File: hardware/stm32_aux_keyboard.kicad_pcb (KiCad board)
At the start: 2 copper layers, 95 x 95 mm, 188 parts, among them J1 I2C_HEADER,2.54, J2 WS2812_HEADER, J3 BUZZER_HEADER, J4 ROT_ENC_HEADER, J5 SWD_SWD, J6 SWD_SWD, J7 ROT_ENC_HEADER, J8 I2C_HEADER,2.54, Q1 SS9013_J3, SW1 USR_BTN_1, SW10 KEY22, SW11 KEY23, SW12 KEY31, SW13 KEY32, SW14 KEY33, SW18 ROT1, SW19 SW_RESET,2_leg,SMD, SW2 USR_BTN_2, SW3 USR_BTN_3, SW5 ROT2, SW6 KEY11, SW7 KEY12, SW8 KEY13, SW9 KEY21, U1 SSD1306-OLED-I2C, U10 STM32F103C8T6, U2 AMS1117-3.3, U3 74AHCT1G125, U4 USB, U5 USBLC6-2SC6_SOT23-6, U6 STM32F103C8T6_rect, U7 SWD, U8 AMS1117-3.3, U9 USBLC6-2SC6_SOT23-6, Y1 O_8M, Y2 O8M, Y3 O32.768K

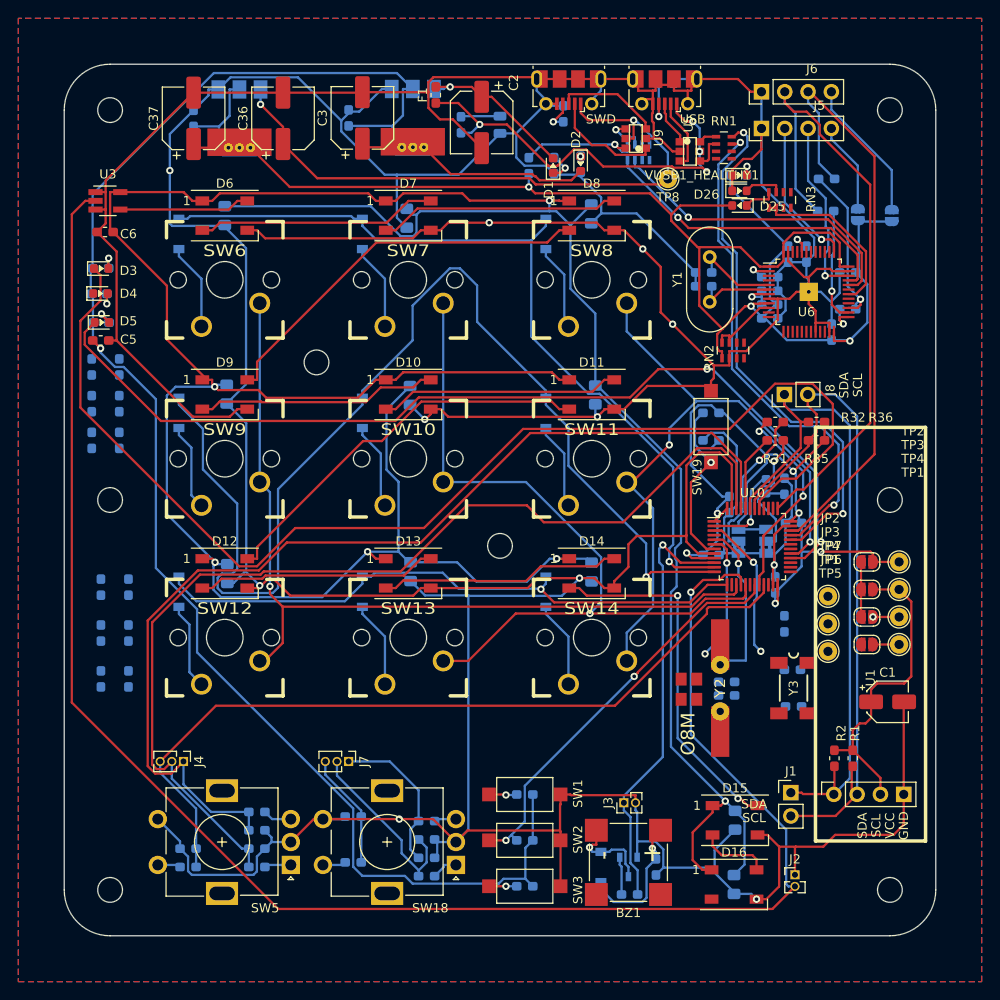
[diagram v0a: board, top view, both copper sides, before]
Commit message: update for tidy tracks,
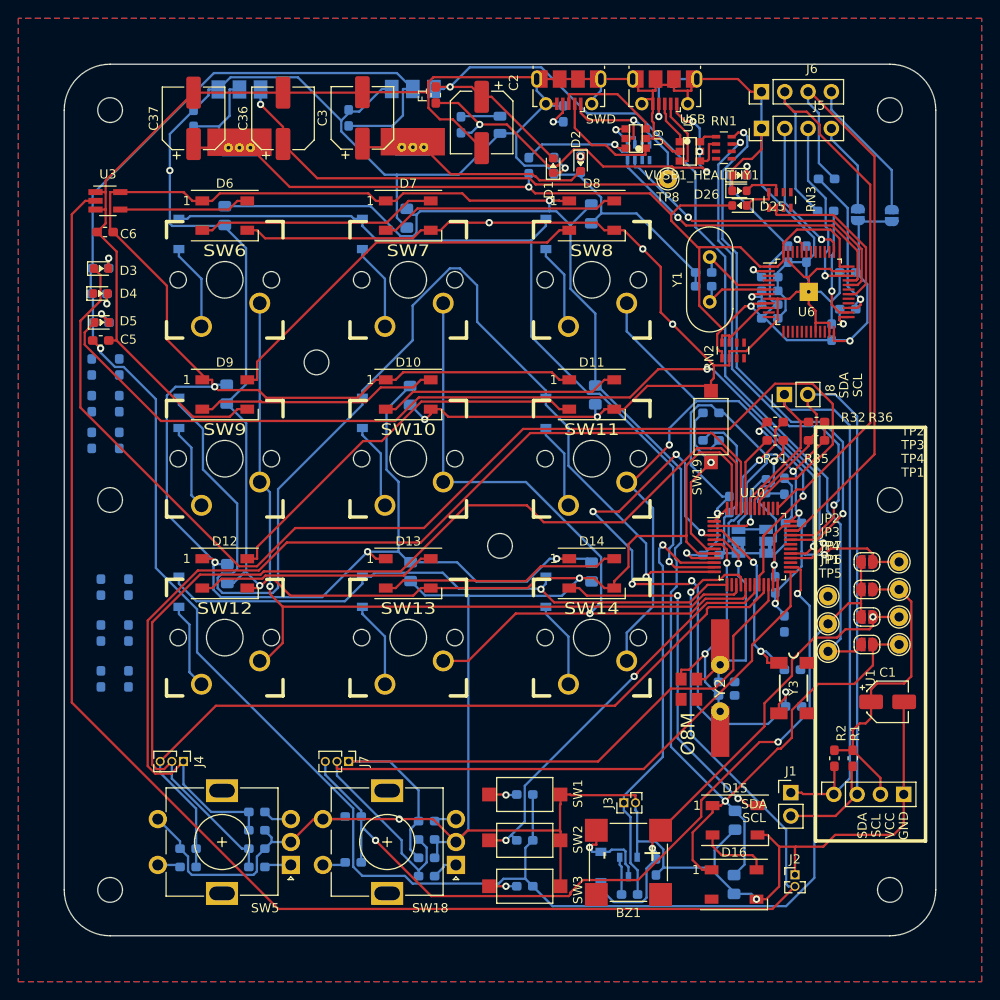
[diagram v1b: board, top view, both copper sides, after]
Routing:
- net +5V: track 18.0 -> 113.6 mm
- net /stm32_core/ROT_ENC_SW2: track 12.6 -> 91.3 mm, vias 0 -> 3
- net /stm32_core/OSC32K_N: track 0.00 -> 68.4 mm, vias 0 -> 6
- net +3V3: track 204.5 -> 270.2 mm
- net /rot_enc/B: track 20.3 -> 82.7 mm
- net /rot_enc/A: track 17.0 -> 74.0 mm
- net Vbuzzer: track 17.7 -> 54.1 mm
- net VCC: track 363.8 -> 390.1 mm
- net /stm32_core/OSC_N: track 14.6 -> 28.1 mm
- net /stm32_core/OSC_P: track 19.7 -> 27.2 mm
- net /stm32_core/OSC32K_P: track 16.0 -> 22.2 mm
- net Vstm32: track 91.4 -> 93.5 mm
- net /keyboard_key/COL3: track 73.8 -> 74.7 mm
- net /stm32_core/USB_P: track 55.2 -> 56.0 mm
- net /status_display/USR_LED_3: track 104.9 -> 105.5 mm
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
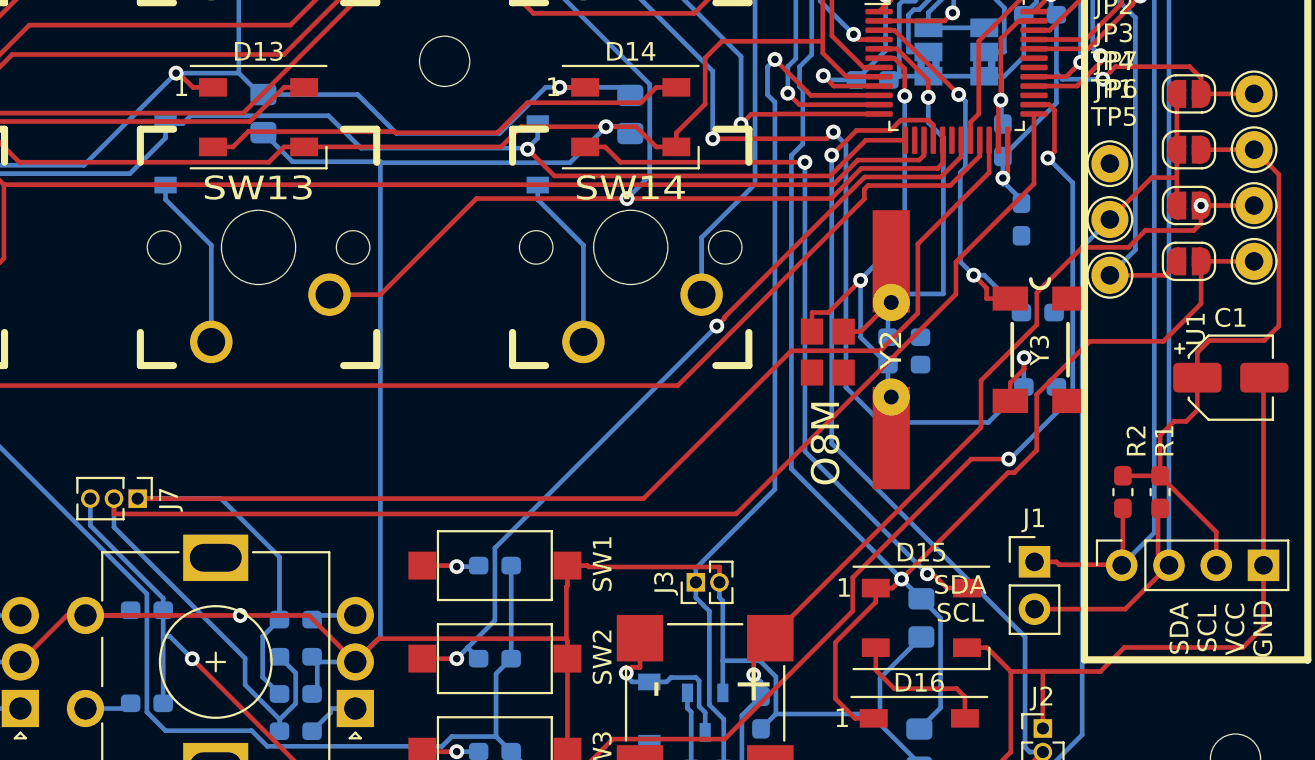
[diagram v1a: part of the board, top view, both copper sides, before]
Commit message: update for tidy tracks,
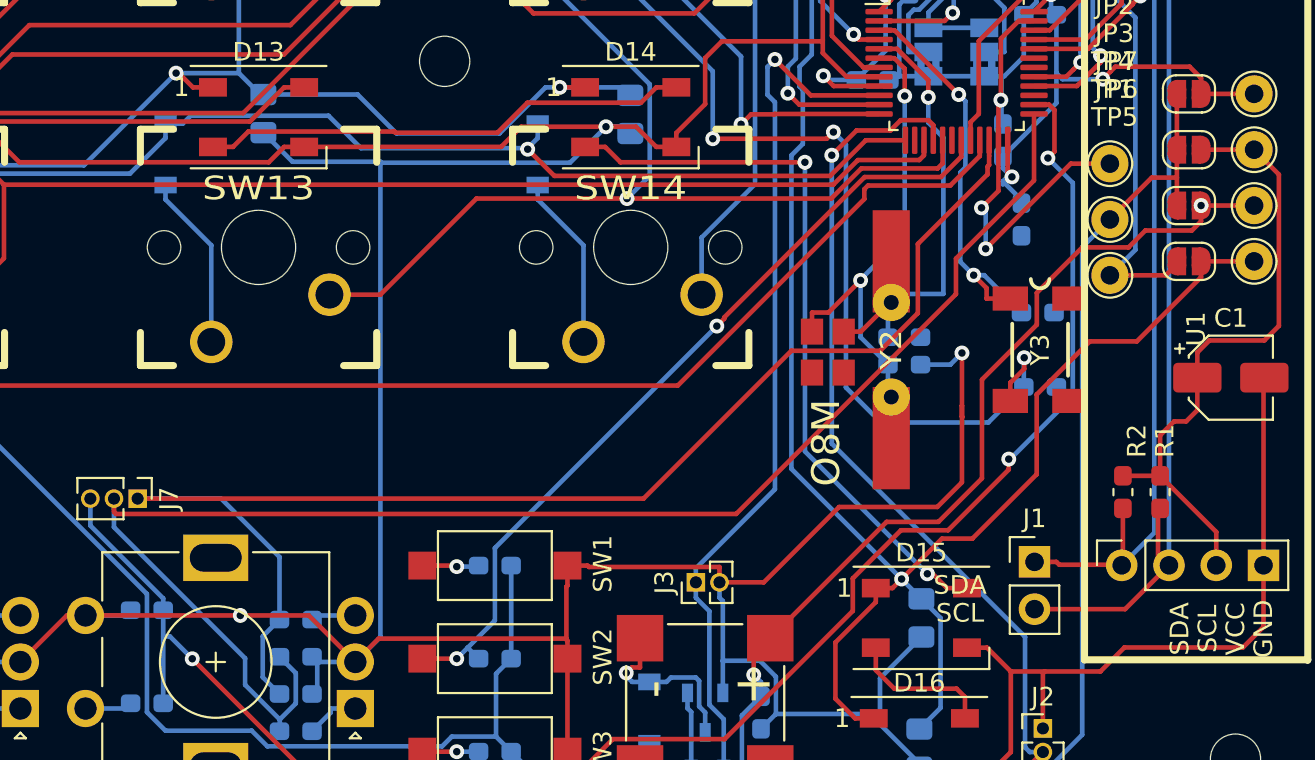
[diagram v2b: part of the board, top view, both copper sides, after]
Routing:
- net GND: track 822.2 -> 862.4 mm, vias 11 -> 14
- net Vbuzzer: track 54.1 -> 55.7 mm

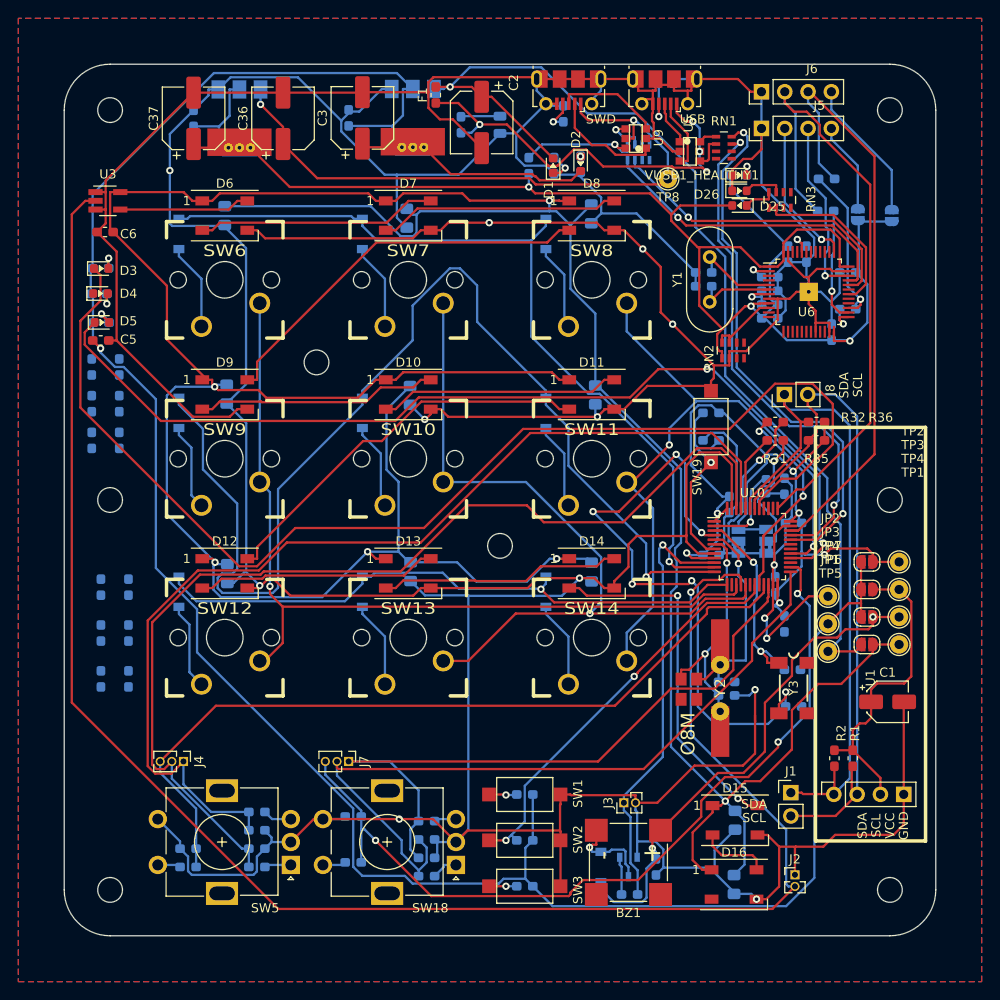
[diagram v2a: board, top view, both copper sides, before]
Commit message: update for tidy tracks,
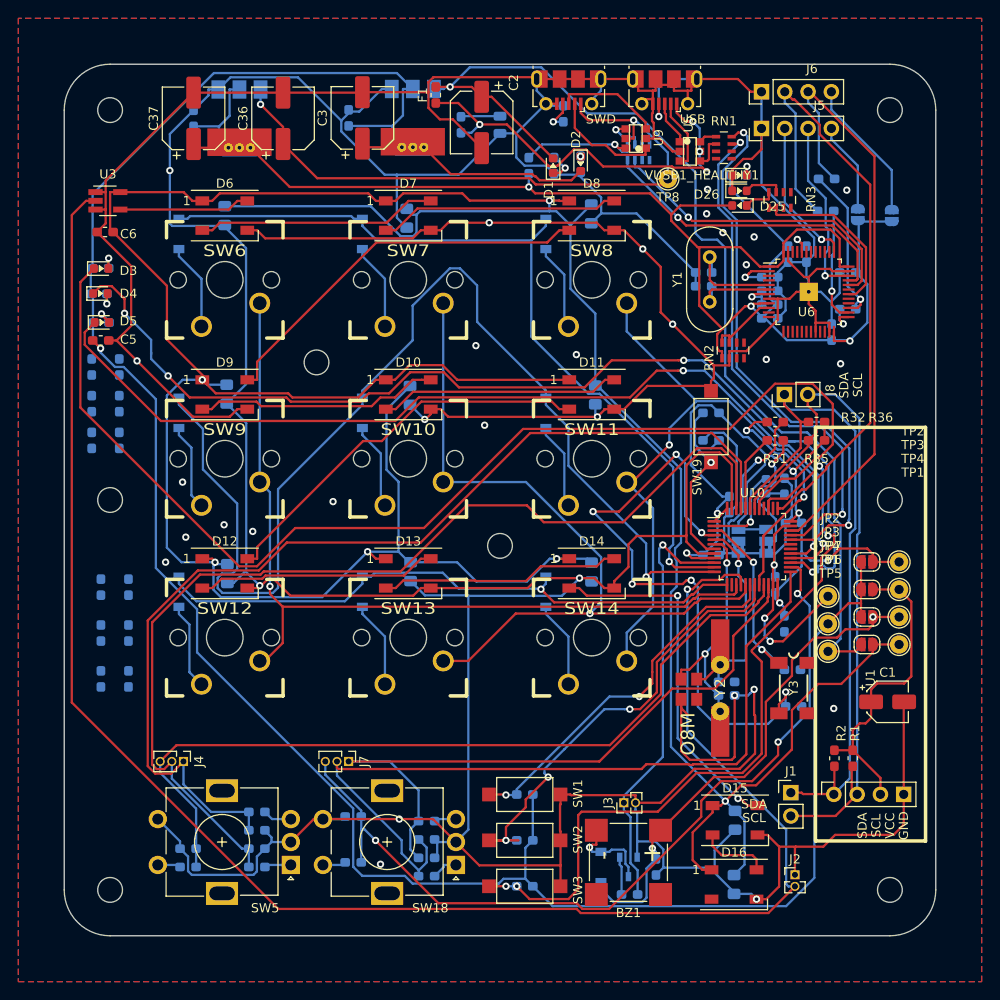
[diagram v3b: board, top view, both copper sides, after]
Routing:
- net /status_display/USR_LED_2: track 0.00 -> 114.5 mm, vias 0 -> 4
- net /stm32_core/USR_BTN3: track 3.03 -> 86.8 mm, vias 1 -> 4
- net /stm32_core/USR_BTN1: track 3.07 -> 40.7 mm, vias 1 -> 2
- net GND: track 862.4 -> 885.3 mm, vias 14 -> 35
- net /stm32_core/USR_BTN2: track 44.2 -> 50.3 mm, vias 2 -> 3
- net /rot_enc/B: track 82.6 -> 88.3 mm
- net VCC: track 390.0 -> 394.0 mm
- net /stm32_core/BOOT1: track 22.3 -> 25.2 mm
- net +5V: track 113.6 -> 116.2 mm
- net /stm32_core/ROT_ENC_SW1: track 87.7 -> 89.6 mm
- net Net-(R19-Pad2): track 3.00 -> 4.66 mm
- net /stm32_core/USB_N: track 58.7 -> 60.3 mm
- net /stm32_core/ROT_ENC_SW2: track 91.6 -> 93.2 mm
- net Net-(C30-Pad2): track 9.47 -> 10.9 mm
- net /WS2812/WS2812_IN: track 190.3 -> 191.4 mm
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
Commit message: update for tidy tracks,
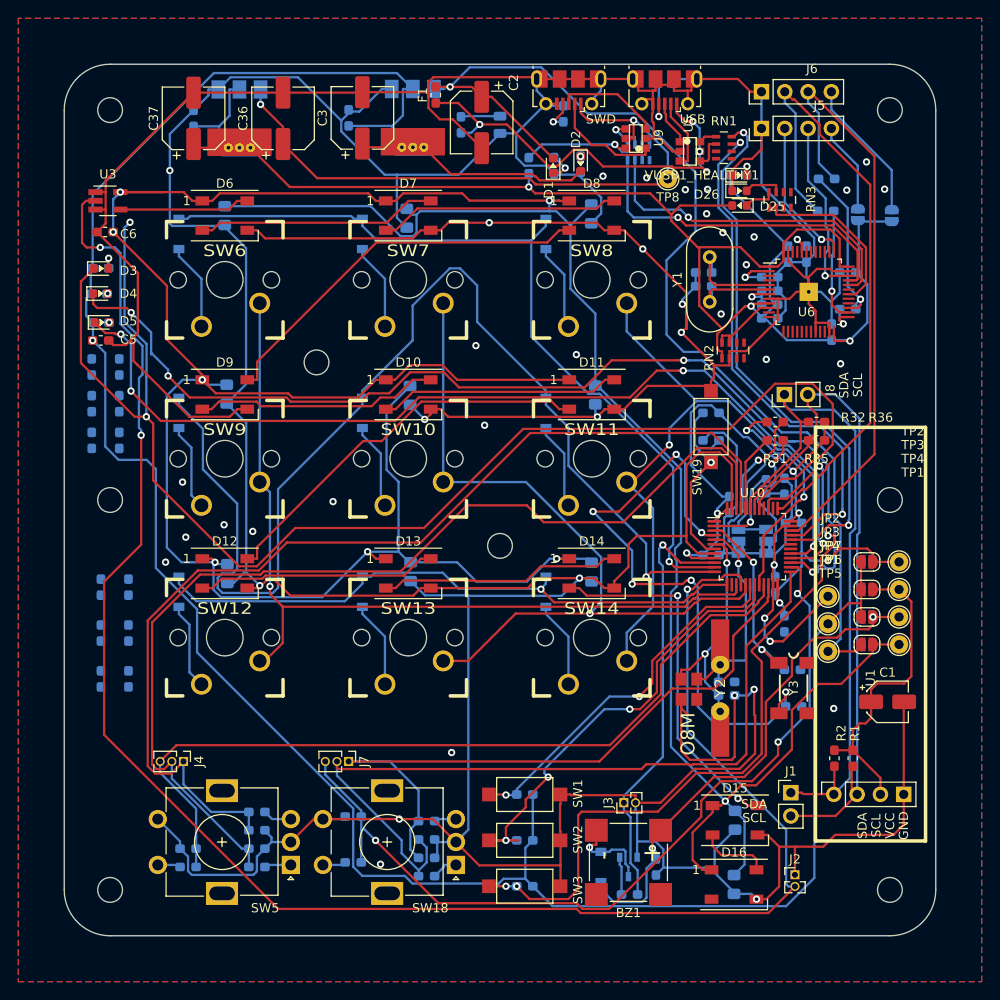
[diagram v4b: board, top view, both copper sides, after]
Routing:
- net /status_display/USR_LED_1: track 129.9 -> 153.0 mm, vias 0 -> 2
- net GND: track 885.3 -> 879.9 mm, vias 35 -> 42
- net /WS2812/WS2812_IN: track 191.4 -> 195.9 mm, vias 1 -> 3
- net VCC: track 394.0 -> 397.7 mm, vias 6 -> 8
- net /stm32_swd/USB_P: track 33.7 -> 36.6 mm
- net +5V: track 116.2 -> 118.9 mm
- net Net-(D5-Pad2): track 2.56 -> 0.04 mm
- net Net-(D4-Pad2): track 2.25 -> 0.11 mm
- net /stm32_swd/USB_N: track 34.3 -> 36.4 mm
- net /status_display/USR_LED_3: vias 2 -> 4

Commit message: update for tidy tracks,
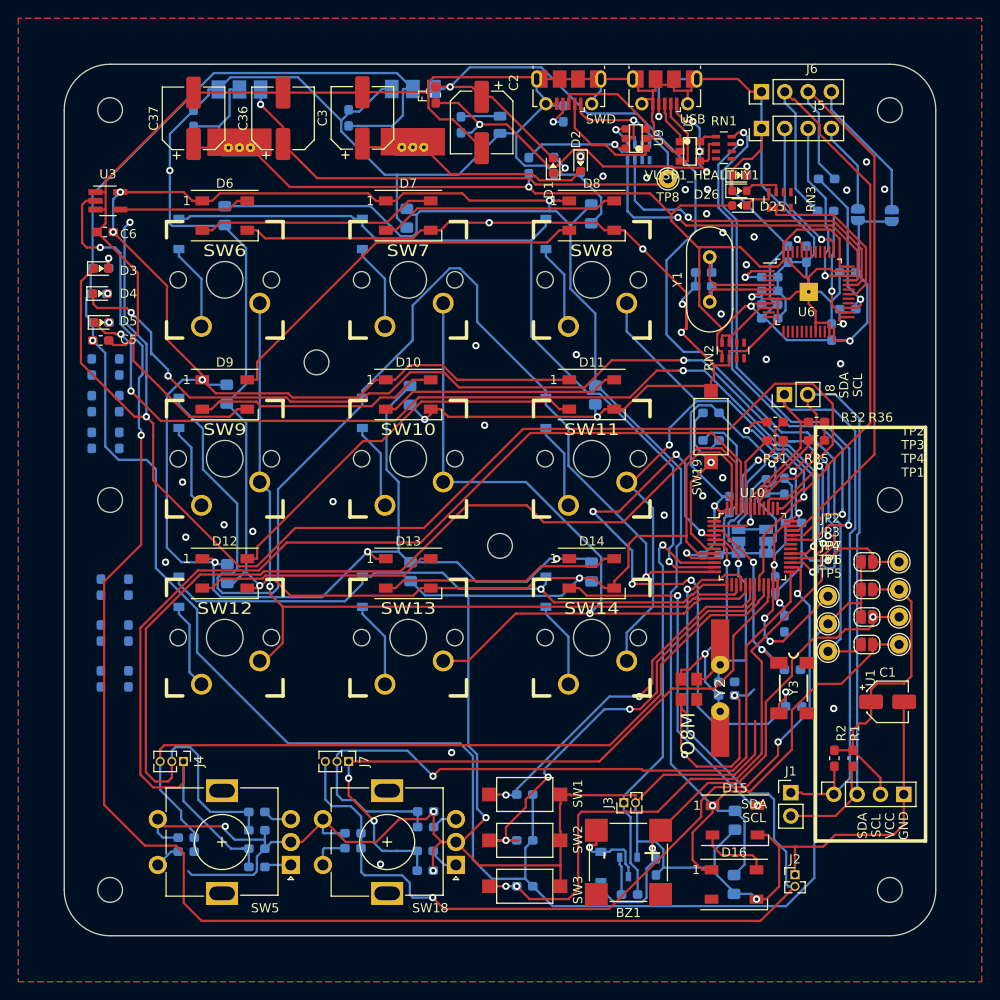
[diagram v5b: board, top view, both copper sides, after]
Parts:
- moved C39 5.05 mm to (59.4, 101.5)
- moved C40 3.40 mm to (59.4, 107.9)
- moved R29 2.75 mm to (59.4, 105.8)
- moved C41 1.83 mm to (51.5, 103.8)
- moved R18 1.69 mm to (33.3, 105.8)
- moved R30 1.55 mm to (51.5, 105.5)
- moved C28 1.22 mm to (33.3, 104.3)
- moved R28 0.66 mm to (59.4, 103.2)
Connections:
- C26 pad 1: /rot_enc2/A -> /rot_enc2/B
- C27 pad 1: /rot_enc2/B -> /rot_enc2/A
- C39 pad 1: /rot_enc/A -> /rot_enc/B
- C40 pad 1: /rot_enc/B -> /rot_enc/A
- R16 pad 2: /rot_enc2/A -> /rot_enc2/B
- R17 pad 2: /rot_enc2/B -> /rot_enc2/A
- R28 pad 2: /rot_enc/A -> /rot_enc/B
- R29 pad 2: /rot_enc/B -> /rot_enc/A
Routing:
- net GND: track 879.9 -> 897.7 mm, vias 42 -> 48
- net /WS2812/WS2812_IN: track 195.9 -> 205.4 mm
- net /rot_enc2/A: track 113.0 -> 120.8 mm
- net /rot_enc2/B: track 112.3 -> 118.0 mm
- net /rot_enc/B: track 88.3 -> 84.7 mm, vias 0 -> 1
- net +3V3: track 270.7 -> 273.9 mm
- net Vstm32: track 93.7 -> 95.6 mm
- net Net-(R30-Pad1): track 2.54 -> 4.14 mm
- net /stm32_core/ROT_ENC_SW2: track 93.2 -> 94.3 mm
- net /stm32_core/ROT_ENC_SW1: track 89.6 -> 88.6 mm
- net VCC: track 397.7 -> 398.7 mm
- net /rot_enc/A: track 74.0 -> 74.7 mm, vias 0 -> 2

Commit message: update for tidy tracks,
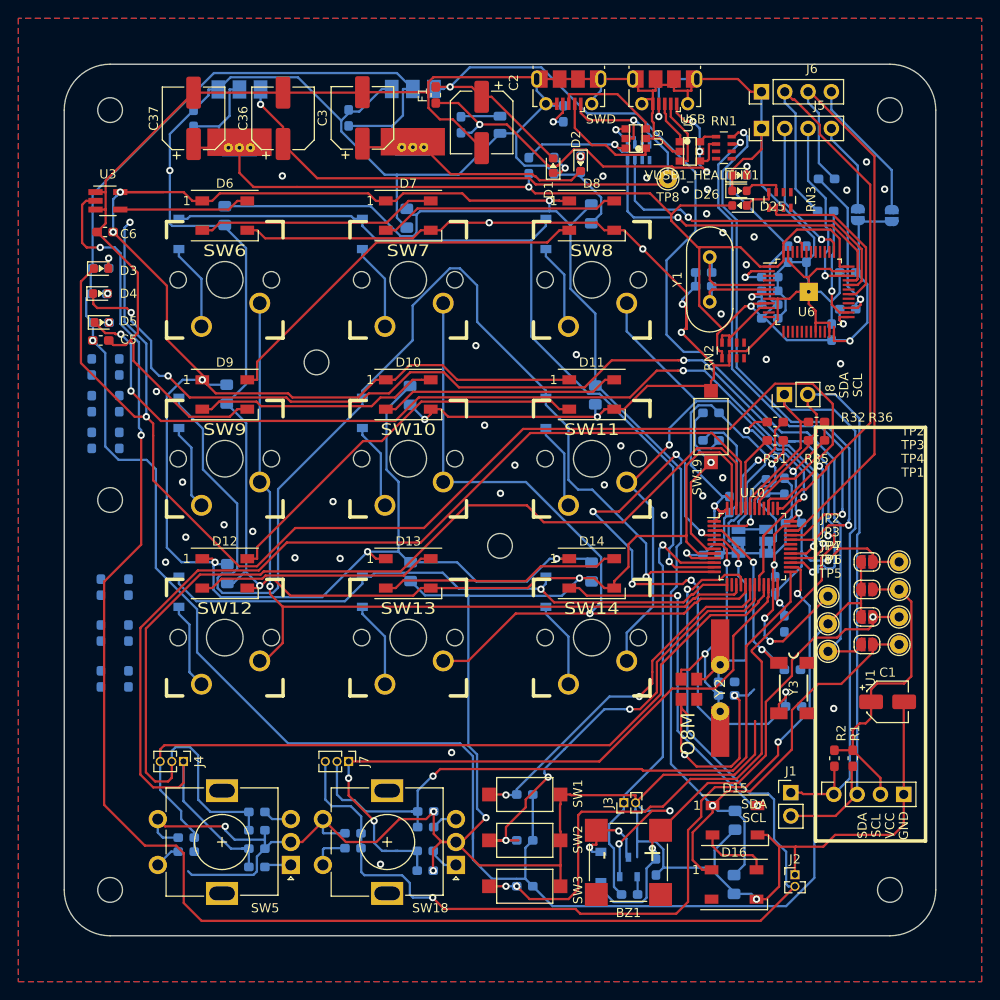
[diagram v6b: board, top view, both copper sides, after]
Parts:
- turned Q1 to 180 degrees
- turned R15 to 180 degrees
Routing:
- net GND: track 897.7 -> 912.5 mm, vias 48 -> 58
- net /rot_enc/B: track 84.7 -> 76.8 mm
- net /stm32_core/ROT_ENC_SW2: track 94.3 -> 99.3 mm
- net Vstm32_stlink: track 177.7 -> 181.2 mm
- net Net-(Q1-Pad1): track 4.14 -> 1.96 mm
- net /keyboard_key/ROW2: track 125.4 -> 126.3 mm
- net /stm32_core/BUZZER: track 47.2 -> 47.8 mm
- net Net-(BZ1-PadN): track 9.72 -> 9.66 mm, vias 1 -> 2
